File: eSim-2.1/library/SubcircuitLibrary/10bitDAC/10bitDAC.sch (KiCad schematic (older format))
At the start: 13 parts, among them U1 PORT, U2 summer

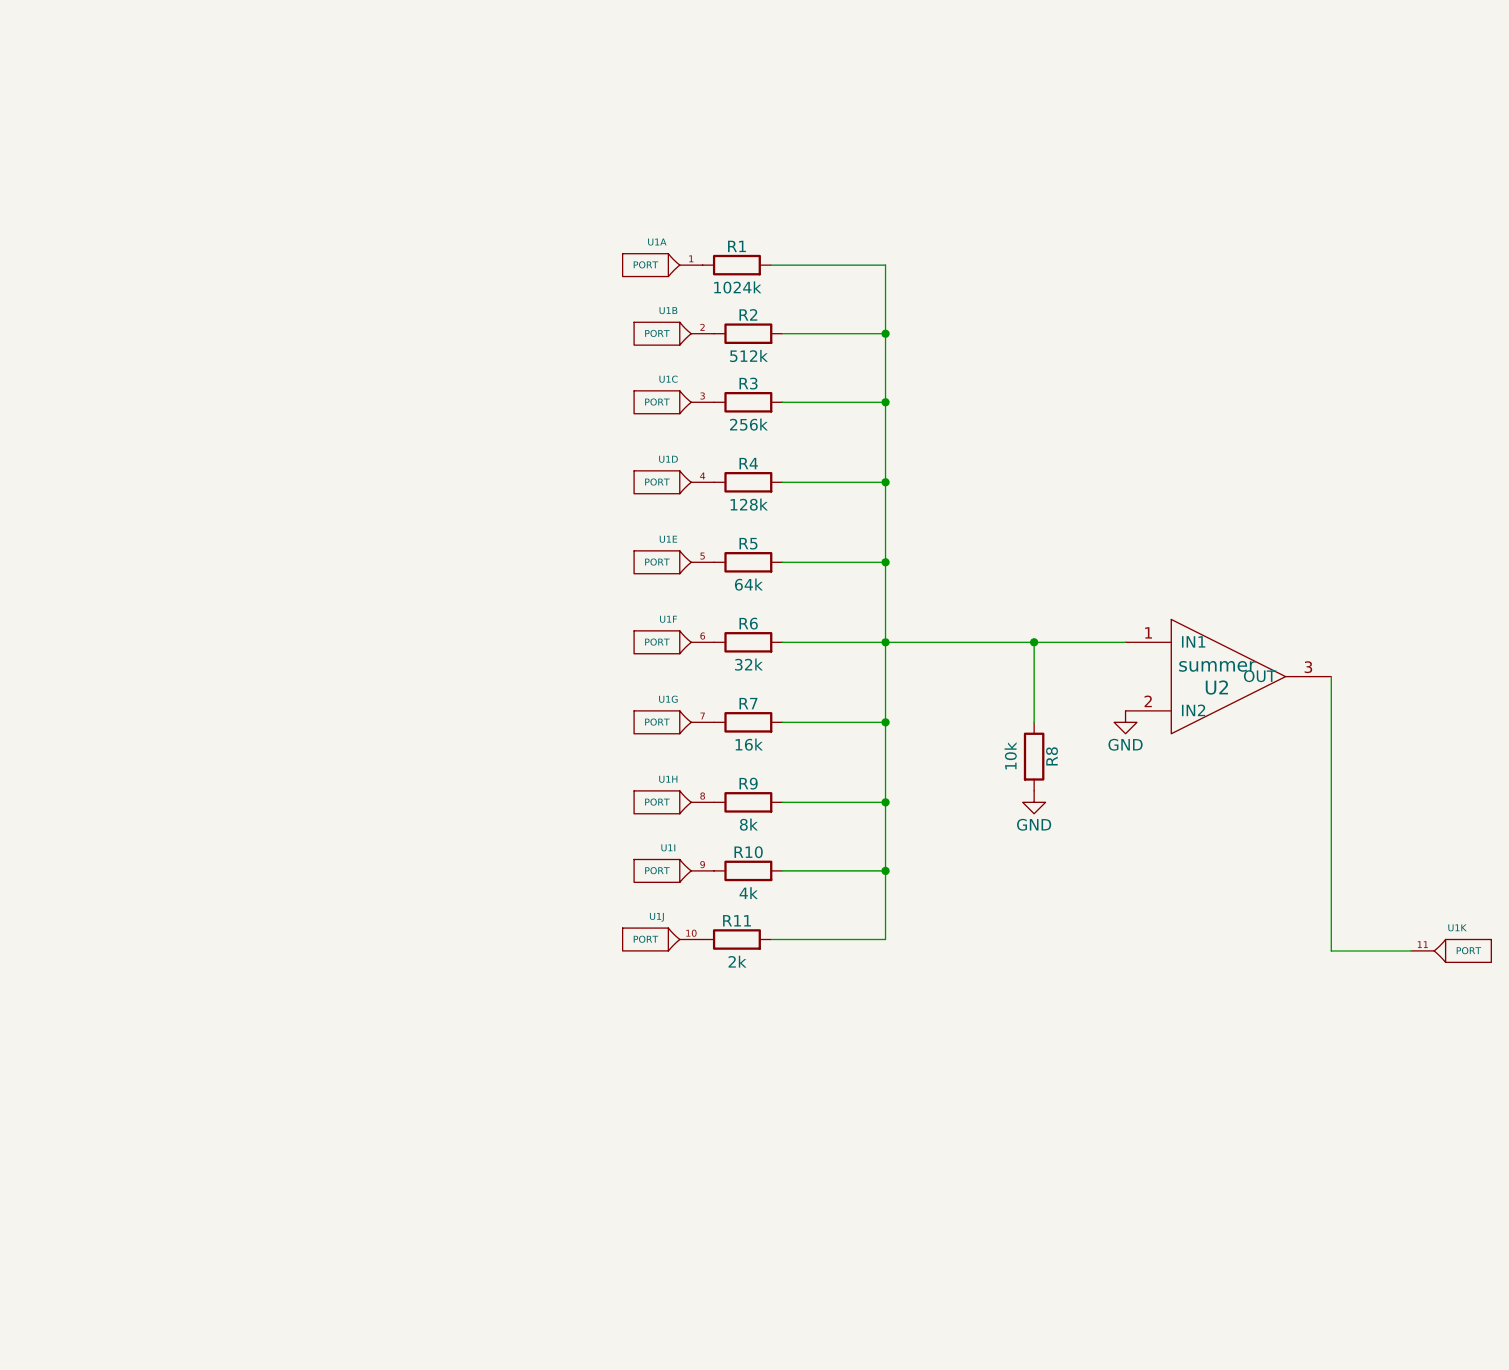
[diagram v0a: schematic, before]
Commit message: Editted Subckt
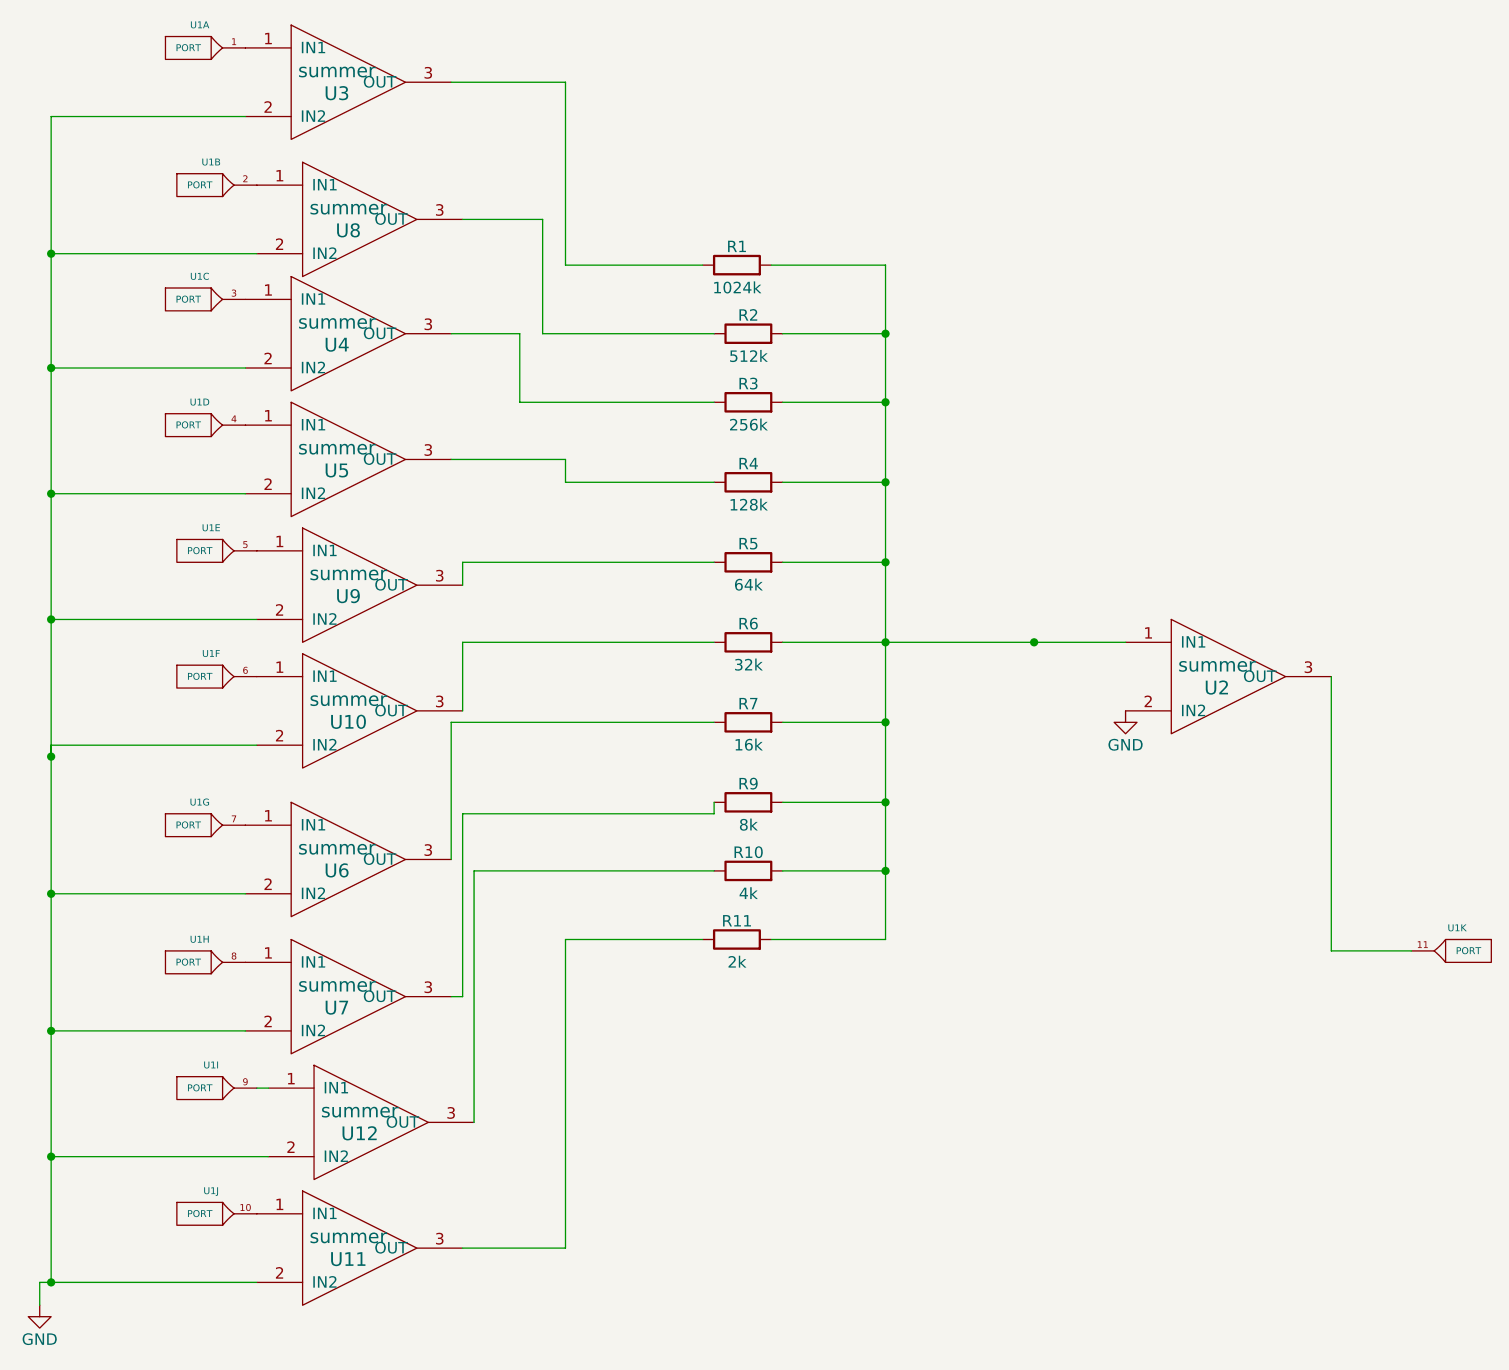
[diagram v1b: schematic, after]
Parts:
- removed R8: 10k, symbol resistor
- added U10, U11, U12, U3, U4, U5, U6, U7, U8, U9: summer, symbol summer
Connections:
- net GND: now also U10.2 (IN2), U11.2 (IN2), U12.2 (IN2), U3.2 (IN2), U4.2 (IN2), U5.2 (IN2), U6.2 (IN2), U7.2 (IN2), U8.2 (IN2), U9.2 (IN2)
- net at R1.1: now also U3.3 (OUT); no longer U1.1
- net at R2.1: now also U8.3 (OUT); no longer U1.2
- net at R3.1: now also U4.3 (OUT); no longer U1.3
- net at R4.1: now also U5.3 (OUT); no longer U1.4
- net at R5.1: now also U9.3 (OUT); no longer U1.5
- net at R6.1: now also U10.3 (OUT); no longer U1.6
- net at R7.1: now also U6.3 (OUT); no longer U1.7
- net at R9.1: now also U7.3 (OUT); no longer U1.8
- net at R10.1: now also U12.3 (OUT); no longer U1.9
- net at R11.1: now also U11.3 (OUT); no longer U1.10
- new net: U1.10, U11.1 (IN1)
- new net: U1.9, U12.1 (IN1)
- new net: U1.8, U7.1 (IN1)
- new net: U1.7, U6.1 (IN1)
- new net: U1.6, U10.1 (IN1)
- new net: U1.5, U9.1 (IN1)
- new net: U1.4, U5.1 (IN1)
- new net: U1.3, U4.1 (IN1)
- new net: U1.2, U8.1 (IN1)
- new net: U1.1, U3.1 (IN1)
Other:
- moved on the sheet: U1A, U1B, U1C, U1D, U1E, U1F, U1G, U1H, U1I, U1J
